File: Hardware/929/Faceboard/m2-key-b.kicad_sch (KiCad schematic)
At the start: 25 parts, among them Q1 2SC4213, U16 TXS0104, U17 TXS0104, U18 SN74CB3Q3245RGYR, U6 Supervisor M2 10128793-001RLF, Y1 25.000MHz

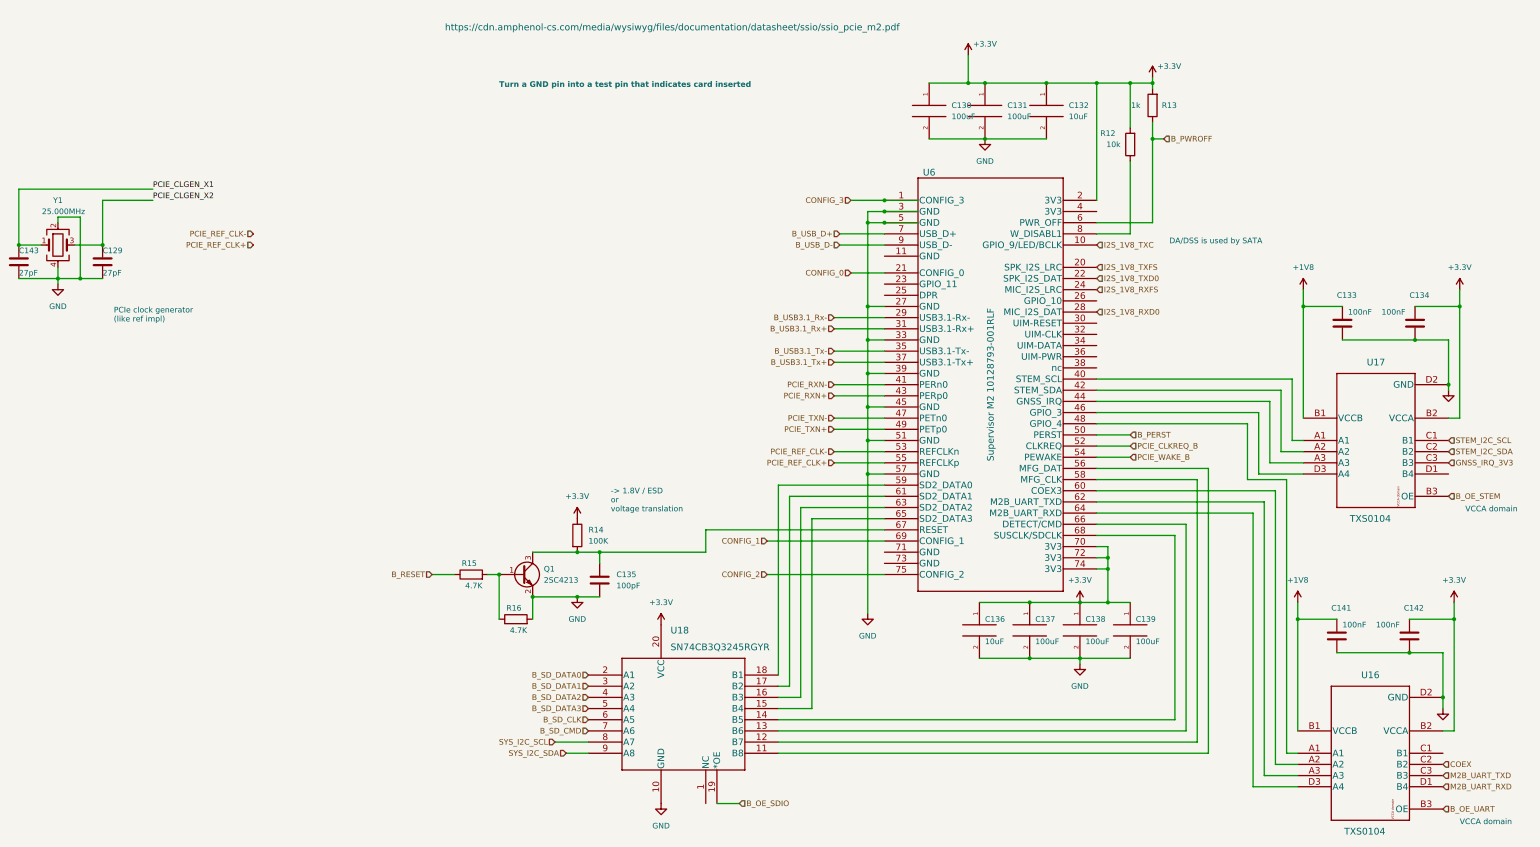
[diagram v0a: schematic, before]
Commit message: Added components
ESD HDMI
Extra components planned
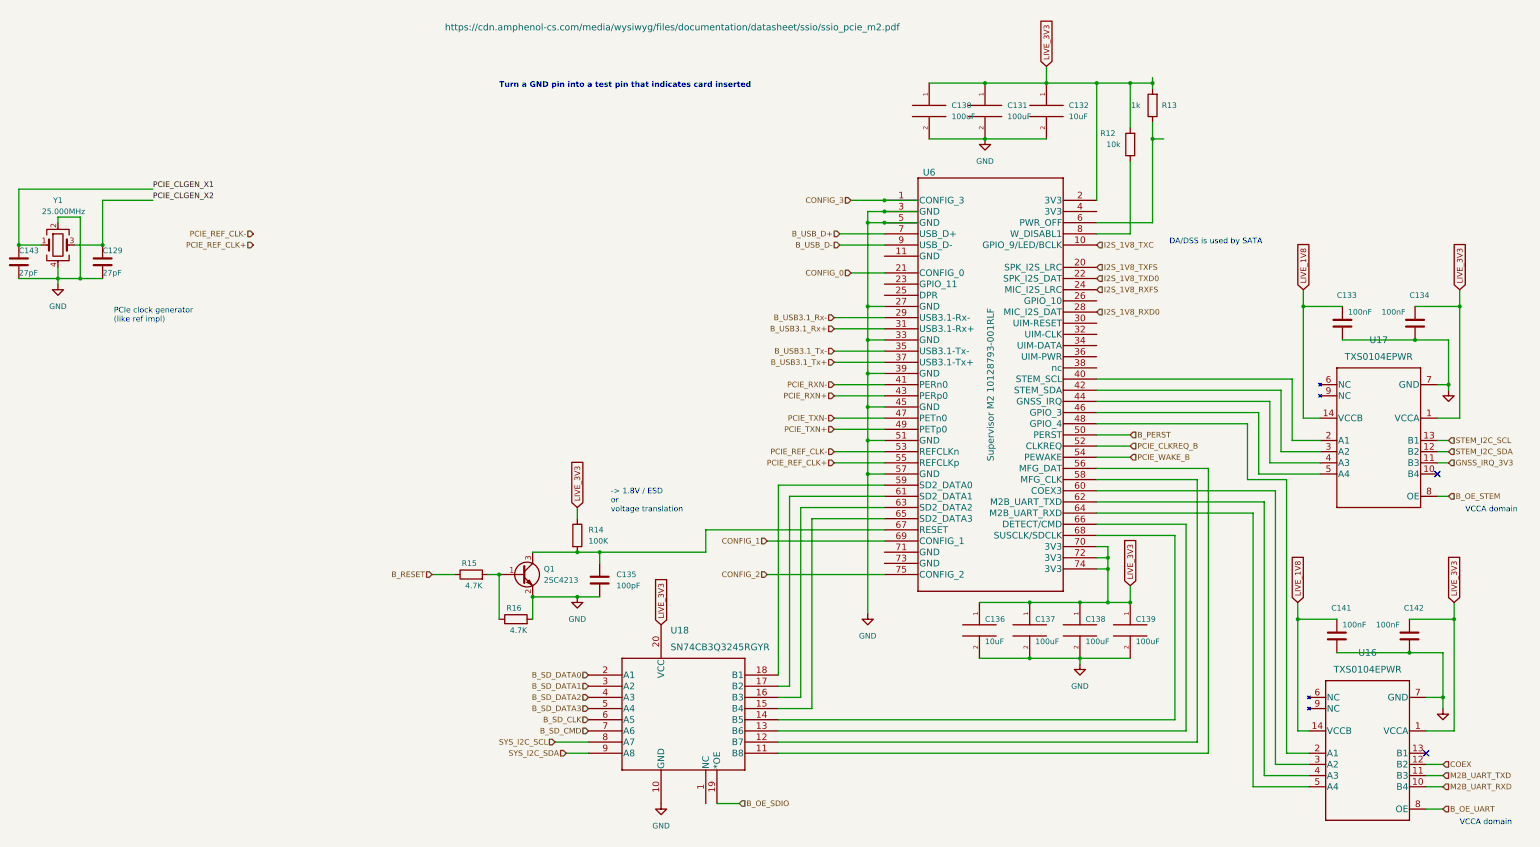
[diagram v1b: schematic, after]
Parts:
- removed U16, U17: TXS0104, Ziloo:TXS0104EYZTR, symbol Ziloo:TXS0104EYZTR
- added U16, U17: TXS0104EPWR, Ziloo:TXS0104EPWR, symbol Ziloo:TXS0104EPWR
- Y1: footprint Crystal:Crystal_HC18-U_Vertical -> Oscillator:Oscillator_SMD_Abracon_ASV-4Pin_7.0x5.1mm_HandSoldering
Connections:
- net B_OE_STEM: now also U17.8 (OE)
- net B_OE_UART: now also U16.8 (OE)
- net COEX: now also U16.12 (B2)
- net GND: now also U16.7 (GND), U17.7 (GND)
- net GNSS_IRQ_3V3: now also U17.11 (B3)
- net M2B_UART_RXD: now also U16.10 (B4)
- net M2B_UART_TXD: now also U16.11 (B3)
- net STEM_I2C_SCL: now also U17.13 (B1)
- net STEM_I2C_SDA: now also U17.12 (B2)
- net at U6.40 (STEM_SCL): now also U17.2 (A1)
- net at U6.42 (STEM_SDA): now also U17.3 (A2)
- net at U6.44 (GNSS_IRQ): now also U17.4 (A3)
- net at U6.46 (GPIO_3): now also U17.5 (A4)
- net at U6.48 (GPIO_4): now also U16.2 (A1)
- net at U6.60 (COEX3): now also U16.3 (A2)
- net at U6.62 (M2B_UART_TXD): now also U16.4 (A3)
- net at U6.64 (M2B_UART_RXD): now also U16.5 (A4)
- net +1V8 renamed LIVE_1V8
- net LIVE_1V8: now also U16.14 (VCCB), U17.14 (VCCB)
- net +3.3V renamed LIVE_3V3
- net LIVE_3V3: now also U16.1 (VCCA), U17.1 (VCCA)
- net B_PWROFF: no longer names the net of R13.1, U6.6 (PWR_OFF)
- no-connect marks 0 -> 2

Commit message: Removed VSOM diodes
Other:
- moved on the sheet: C129, C143, Y1
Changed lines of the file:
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@@
   (junction (at 322.58 40.64) (diameter 0) (color 0 0 0 0)
   )
-  (junction (at 64.77 64.77) (diameter 0) (color 0 0 0 0)
+  (junction (at 160.02 73.66) (diameter 0) (color 0 0 0 0)
   )
   (junction (at 317.5 27.94) (diameter 0) (color 0 0 0 0)
   )
-  (junction (at 73.66 72.39) (diameter 0) (color 0 0 0 0)
+  (junction (at 168.91 81.28) (diameter 0) (color 0 0 0 0)
   )
   (junction (at 306.07 146.05) (diameter 0) (color 0 0 0 0)
@@
   (junction (at 261.62 59.69) (diameter 0) (color 0 0 0 0)
   )
-  (junction (at 83.82 64.77) (diameter 0) (color 0 0 0 0)
+  (junction (at 179.07 73.66) (diameter 0) (color 0 0 0 0)
   )
   (junction (at 392.43 78.74) (diameter 0) (color 0 0 0 0)
@@
   (junction (at 257.81 109.22) (diameter 0) (color 0 0 0 0)
   )
-  (junction (at 78.74 72.39) (diameter 0) (color 0 0 0 0)
+  (junction (at 173.99 81.28) (diameter 0) (color 0 0 0 0)
   )
   (junction (at 309.88 27.94) (diameter 0) (color 0 0 0 0)
@@
     (stroke (width 0) (type default) (color 0 0 0 0))
   )
-  (wire (pts (xy 78.74 72.39) (xy 83.82 72.39))
+  (wire (pts (xy 173.99 81.28) (xy 179.07 81.28))
     (stroke (width 0) (type default) (color 0 0 0 0))
   )
@@
     (stroke (width 0) (type default) (color 0 0 0 0))
   )
-  (wire (pts (xy 83.82 54.61) (xy 95.25 54.61))
+  (wire (pts (xy 179.07 63.5) (xy 190.5 63.5))
     (stroke (width 0) (type default) (color 0 0 0 0))
   )
@@
     (stroke (width 0) (type default) (color 0 0 0 0))
   )
-  (wire (pts (xy 64.77 72.39) (xy 73.66 72.39))
+  (wire (pts (xy 160.02 81.28) (xy 168.91 81.28))
     (stroke (width 0) (type default) (color 0 0 0 0))
   )
@@
     (stroke (width 0) (type default) (color 0 0 0 0))
   )
-  (wire (pts (xy 64.77 64.77) (xy 64.77 52.07))
+  (wire (pts (xy 160.02 73.66) (xy 160.02 60.96))
     (stroke (width 0) (type default) (color 0 0 0 0))
   )
@@
     (stroke (width 0) (type default) (color 0 0 0 0))
   )
-  (wire (pts (xy 73.66 59.69) (xy 73.66 58.42))
+  (wire (pts (xy 168.91 68.58) (xy 168.91 67.31))
     (stroke (width 0) (type default) (color 0 0 0 0))
   )
@@
     (stroke (width 0) (type default) (color 0 0 0 0))
   )
-  (wire (pts (xy 78.74 58.42) (xy 78.74 72.39))
+  (wire (pts (xy 173.99 67.31) (xy 173.99 81.28))
     (stroke (width 0) (type default) (color 0 0 0 0))
   )
@@
     (stroke (width 0) (type default) (color 0 0 0 0))
   )
-  (wire (pts (xy 64.77 64.77) (xy 69.85 64.77))
+  (wire (pts (xy 160.02 73.66) (xy 165.1 73.66))
     (stroke (width 0) (type default) (color 0 0 0 0))
   )
@@
     (stroke (width 0) (type default) (color 0 0 0 0))
   )
-  (wire (pts (xy 73.66 72.39) (xy 73.66 73.66))
+  (wire (pts (xy 168.91 81.28) (xy 168.91 82.55))
     (stroke (width 0) (type default) (color 0 0 0 0))
   )
@@
     (stroke (width 0) (type default) (color 0 0 0 0))
   )
-  (wire (pts (xy 73.66 69.85) (xy 73.66 72.39))
+  (wire (pts (xy 168.91 78.74) (xy 168.91 81.28))
     (stroke (width 0) (type default) (color 0 0 0 0))
   )
-  (wire (pts (xy 73.66 58.42) (xy 78.74 58.42))
+  (wire (pts (xy 168.91 67.31) (xy 173.99 67.31))
     (stroke (width 0) (type default) (color 0 0 0 0))
   )
@@
     (stroke (width 0) (type default) (color 0 0 0 0))
   )
-  (wire (pts (xy 64.77 52.07) (xy 95.25 52.07))
+  (wire (pts (xy 160.02 60.96) (xy 190.5 60.96))
     (stroke (width 0) (type default) (color 0 0 0 0))
   )
@@
     (stroke (width 0) (type default) (color 0 0 0 0))
   )
-  (wire (pts (xy 78.74 72.39) (xy 73.66 72.39))
+  (wire (pts (xy 173.99 81.28) (xy 168.91 81.28))
     (stroke (width 0) (type default) (color 0 0 0 0))
   )
@@
     (stroke (width 0) (type default) (color 0 0 0 0))
   )
-  (wire (pts (xy 77.47 64.77) (xy 83.82 64.77))
+  (wire (pts (xy 172.72 73.66) (xy 179.07 73.66))
     (stroke (width 0) (type default) (color 0 0 0 0))
   )
@@
     (stroke (width 0) (type default) (color 0 0 0 0))
   )
-  (wire (pts (xy 83.82 64.77) (xy 83.82 54.61))
+  (wire (pts (xy 179.07 73.66) (xy 179.07 63.5))
     (stroke (width 0) (type default) (color 0 0 0 0))
   )
@@
     (effects (font (size 1.27 1.27) bold) (justify left bottom))
   )
-  (text "PCIe clock generator \n(like ref impl)\n" (at 86.36 82.55 0)
+  (text "PCIe clock generator \n(like ref impl)\n" (at 181.61 91.44 0)
     (effects (font (size 1.27 1.27)) (justify left bottom))
   )
@@
     (effects (font (size 1.27 1.27)) (justify left bottom))
   )
-  (label "PCIE_CLGEN_X2" (at 95.25 54.61 0)
+  (label "PCIE_CLGEN_X2" (at 190.5 63.5 0)
     (effects (font (size 1.27 1.27)) (justify left bottom))
   )
-  (label "PCIE_CLGEN_X1" (at 95.25 52.07 0)
+  (label "PCIE_CLGEN_X1" (at 190.5 60.96 0)
     (effects (font (size 1.27 1.27)) (justify left bottom))
   )
@@
     (effects (font (size 1.27 1.27)) (justify right))
   )
-  (hierarchical_label "PCIE_REF_CLK+" (shape input) (at 118.11 64.77 180)
+  (hierarchical_label "PCIE_REF_CLK+" (shape input) (at 213.36 73.66 180)
     (effects (font (size 1.27 1.27)) (justify right))
   )
-  (hierarchical_label "PCIE_REF_CLK-" (shape input) (at 118.11 62.23 180)
+  (hierarchical_label "PCIE_REF_CLK-" (shape input) (at 213.36 71.12 180)
     (effects (font (size 1.27 1.27)) (justify right))
   )
@@
     (pin "9")
   )
-  (symbol (lib_id "power:GND") (at 73.66 73.66 0) (unit 1)
+  (symbol (lib_id "power:GND") (at 168.91 82.55 0) (unit 1)
     (in_bom yes) (on_board yes) (fields_autoplaced)
-    (property "Reference" "#PWR0178" (id 0) (at 73.66 80.01 0)
+    (property "Reference" "#PWR0178" (id 0) (at 168.91 88.9 0)
       (effects (font (size 1.27 1.27)) hide)
     )
-    (property "Value" "GND" (id 1) (at 73.66 78.74 0))
-    (property "Footprint" "" (id 2) (at 73.66 73.66 0)
+    (property "Value" "GND" (id 1) (at 168.91 87.63 0))
+    (property "Footprint" "" (id 2) (at 168.91 82.55 0)
       (effects (font (size 1.27 1.27)) hide)
     )
-    (property "Datasheet" "" (id 3) (at 73.66 73.66 0)
+    (property "Datasheet" "" (id 3) (at 168.91 82.55 0)
       (effects (font (size 1.27 1.27)) hide)
     )
@@
     (pin "9")
   )
-  (symbol (lib_id "Device:C") (at 83.82 68.58 0) (unit 1)
+  (symbol (lib_id "Device:C") (at 179.07 77.47 0) (unit 1)
     (in_bom yes) (on_board yes)
-    (property "Reference" "C129" (id 0) (at 83.82 66.04 0)
+    (property "Reference" "C129" (id 0) (at 179.07 74.93 0)
       (effects (font (size 1.27 1.27)) (justify left))
     )
-    (property "Value" "27pF" (id 1) (at 83.82 71.12 0)
+    (property "Value" "27pF" (id 1) (at 179.07 80.01 0)
       (effects (font (size 1.27 1.27)) (justify left))
     )
-    (property "Footprint" "Capacitor_SMD:C_0402_1005Metric" (id 2) (at 84.7852 72.39 0)
+    (property "Footprint" "Capacitor_SMD:C_0402_1005Metric" (id 2) (at 180.0352 81.28 0)
       (effects (font (size 1.27 1.27)) hide)
     )
-    (property "Datasheet" "~" (id 3) (at 83.82 68.58 0)
+    (property "Datasheet" "~" (id 3) (at 179.07 77.47 0)
       (effects (font (size 1.27 1.27)) hide)
     )
@@
     (pin "2")
   )
-  (symbol (lib_id "Device:Crystal_GND24") (at 73.66 64.77 0) (unit 1)
+  (symbol (lib_id "Device:Crystal_GND24") (at 168.91 73.66 0) (unit 1)
     (in_bom yes) (on_board yes)
-    (property "Reference" "Y1" (id 0) (at 73.66 54.61 0))
-    (property "Value" "25.000MHz" (id 1) (at 74.93 57.15 0))
-    (property "Footprint" "Oscillator:Oscillator_SMD_Abracon_ASV-4Pin_7.0x5.1mm_HandSoldering" (id 2) (at 73.66 64.77 0)
+    (property "Reference" "Y1" (id 0) (at 168.91 63.5 0))
+    (property "Value" "25.000MHz" (id 1) (at 170.18 66.04 0))
+    (property "Footprint" "Oscillator:Oscillator_SMD_Abracon_ASV-4Pin_7.0x5.1mm_HandSoldering" (id 2) (at 168.91 73.66 0)
       (effects (font (size 1.27 1.27)) hide)
     )
-    (property "Datasheet" "~" (id 3) (at 73.66 64.77 0)
+    (property "Datasheet" "~" (id 3) (at 168.91 73.66 0)
       (effects (font (size 1.27 1.27)) hide)
     )
@@
     (pin "4")
   )
-  (symbol (lib_id "Device:C") (at 64.77 68.58 0) (unit 1)
+  (symbol (lib_id "Device:C") (at 160.02 77.47 0) (unit 1)
     (in_bom yes) (on_board yes)
-    (property "Reference" "C143" (id 0) (at 64.77 66.04 0)
+    (property "Reference" "C143" (id 0) (at 160.02 74.93 0)
       (effects (font (size 1.27 1.27)) (justify left))
     )
-    (property "Value" "27pF" (id 1) (at 64.77 71.12 0)
+    (property "Value" "27pF" (id 1) (at 160.02 80.01 0)
       (effects (font (size 1.27 1.27)) (justify left))
     )
-    (property "Footprint" "Capacitor_SMD:C_0402_1005Metric" (id 2) (at 65.7352 72.39 0)
+    (property "Footprint" "Capacitor_SMD:C_0402_1005Metric" (id 2) (at 160.9852 81.28 0)
       (effects (font (size 1.27 1.27)) hide)
     )
-    (property "Datasheet" "~" (id 3) (at 64.77 68.58 0)
+    (property "Datasheet" "~" (id 3) (at 160.02 77.47 0)
       (effects (font (size 1.27 1.27)) hide)
     )
